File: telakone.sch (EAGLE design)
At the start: 180 parts, among them X10 MPT0.5/8-2.54, X11 MPT0.5/8-2.54, X2 MPT0.5/8-2.54, X3 MPT0.5/8-2.54, X4 PIIKKIRIMA-2, X5 PIIKKIRIMA-5, X7 U.FL-R-SMT-1, X8 MPT0.5/8-2.54, Y1 PTH2.6-5.5SQ, Y2 PTH2.6-5.5SQ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

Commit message: Layout finished
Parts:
- added H1: RED, omat_ic_2:LEDCHIP-LED0603
- added H2, H3: GRN, omat_ic_2:LEDCHIP-LED0603
- added R18, R24, R25: (no value), omat_ic_2:RES0603
- added U$1: DAFUG, dafug:DAFUG
- added X9: PIIKKIRIMA-3, omat_ic_2:PIIKKIRIMA-3
- added Y5: PTH2.6-5.5SQ, EKE:PTH2.6-5.5SQ
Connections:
- new net N$23: H2.C, R24.2
- new net N$25: H1.C, R18.2
- new net N$26: D1G$2.PB8, H1.A
- new net N$27: D1G$2.PB9, H2.A
- new net N$28: H3.C, R25.2
- new net USART1CTS: A1.UART1_RTSL, D1G$2.PA11
- new net USART1RTS: A1.UART1_CTSL, D1G$2.PA12
- new net USART1RX: A1.UART1_TX, D1G$2.PA10
- new net USART1TX: A1.UART1_RX, D1G$2.PA9
- new net USART3RX: D1G$2.PD9, X9.2
- new net USART3TX: D1G$2.PD8, X9.3
- net +3V3: now also H3.A
- net GND: now also R18.1, R24.1, R25.1, X9.1, Y5.1
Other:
- note added: "USART1"
- note added: "USART3"
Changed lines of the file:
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@@
 <part name="GND46" library="EKE" deviceset="GND" device=""/>
 <part name="+3V8" library="EKE" deviceset="+3V3" device=""/>
+<part name="X9" library="omat_ic_2" deviceset="PIIKKIRIMA-3" device=""/>
+<part name="GND85" library="EKE" deviceset="GND" device=""/>
+<part name="H1" library="omat_ic_2" deviceset="LED" device="CHIP-LED0603" value="RED"/>
+<part name="H2" library="omat_ic_2" deviceset="LED" device="CHIP-LED0603" value="GRN"/>
+<part name="R18" library="omat_ic_2" deviceset="RES" device="0603"/>
+<part name="R24" library="omat_ic_2" deviceset="RES" device="0603"/>
+<part name="GND86" library="EKE" deviceset="GND" device=""/>
+<part name="GND87" library="EKE" deviceset="GND" device=""/>
+<part name="H3" library="omat_ic_2" deviceset="LED" device="CHIP-LED0603" value="GRN"/>
+<part name="R25" library="omat_ic_2" deviceset="RES" device="0603"/>
+<part name="GND88" library="EKE" deviceset="GND" device=""/>
+<part name="+3V23" library="EKE" deviceset="+3V3" device=""/>
+<part name="U$1" library="dafug" deviceset="DAFUG" device=""/>
+<part name="Y5" library="EKE" deviceset="PTH" device="2.6-5.5SQ"/>
+<part name="U$2" library="dafug" deviceset="OSHW" device=""/>
 </parts>
 <sheets>
@@
 <instance part="Y3" gate="G$1" x="106.68" y="35.56"/>
 <instance part="Y4" gate="G$1" x="106.68" y="25.4"/>
-<instance part="GND77" gate="1" x="96.52" y="20.32"/>
+<instance part="GND77" gate="1" x="96.52" y="10.16"/>
+<instance part="U$1" gate="G$1" x="292.1" y="30.48"/>
+<instance part="Y5" gate="G$1" x="106.68" y="15.24"/>
+<instance part="U$2" gate="G$1" x="320.04" y="40.64"/>
 </instances>
 <busses>
@@
 <wire x1="96.52" y1="45.72" x2="96.52" y2="35.56" width="0.1524" layer="91"/>
 <wire x1="96.52" y1="35.56" x2="96.52" y2="25.4" width="0.1524" layer="91"/>
-<wire x1="96.52" y1="25.4" x2="96.52" y2="22.86" width="0.1524" layer="91"/>
+<wire x1="96.52" y1="25.4" x2="96.52" y2="15.24" width="0.1524" layer="91"/>
+<wire x1="96.52" y1="15.24" x2="96.52" y2="12.7" width="0.1524" layer="91"/>
 <wire x1="99.06" y1="25.4" x2="96.52" y2="25.4" width="0.1524" layer="91"/>
 <junction x="96.52" y="25.4"/>
@@
 <wire x1="99.06" y1="45.72" x2="96.52" y2="45.72" width="0.1524" layer="91"/>
 <junction x="96.52" y="45.72"/>
+<pinref part="Y5" gate="G$1" pin="1"/>
+<wire x1="99.06" y1="15.24" x2="96.52" y2="15.24" width="0.1524" layer="91"/>
+<junction x="96.52" y="15.24"/>
 </segment>
 </net>
@@
 <text x="251.46" y="193.04" size="1.778" layer="97">TIM9_CH1
 TIM9_CH2</text>
-<text x="88.9" y="147.32" size="1.778" layer="97">SPI2</text>
+<text x="88.9" y="144.78" size="1.778" layer="97">SPI2</text>
 <text x="203.2" y="185.42" size="1.778" layer="97">SPI3</text>
 <text x="88.9" y="162.56" size="1.778" layer="97">I2C1</text>
@@
 <text x="200.66" y="139.7" size="1.778" layer="97">TIM4_CH2</text>
 <text x="200.66" y="160.02" size="1.778" layer="97">USART2</text>
+<text x="86.36" y="185.42" size="1.778" layer="97">USART1</text>
+<text x="236.22" y="144.78" size="1.778" layer="97" rot="R90">USART3</text>
 </plain>
 <instances>
@@
 <instance part="GND53" gate="1" x="200.66" y="53.34"/>
 <instance part="+3V31" gate="G$1" x="200.66" y="66.04"/>
+<instance part="X9" gate="G$1" x="226.06" y="149.86" rot="R180"/>
+<instance part="GND85" gate="1" x="218.44" y="142.24"/>
+<instance part="H1" gate="G$1" x="71.12" y="149.86"/>
+<instance part="H2" gate="G$1" x="81.28" y="149.86"/>
+<instance part="R18" gate="G$1" x="71.12" y="139.7" rot="R90"/>
+<instance part="R24" gate="G$1" x="81.28" y="139.7" rot="R90"/>
+<instance part="GND86" gate="1" x="71.12" y="132.08"/>
+<instance part="GND87" gate="1" x="81.28" y="132.08"/>
+<instance part="H3" gate="G$1" x="60.96" y="149.86"/>
+<instance part="R25" gate="G$1" x="60.96" y="139.7" rot="R90"/>
+<instance part="GND88" gate="1" x="60.96" y="132.08"/>
+<instance part="+3V23" gate="G$1" x="60.96" y="160.02"/>
 </instances>
 <busses>
@@
 <pinref part="GND53" gate="1" pin="GND"/>
 </segment>
+<segment>
+<pinref part="X9" gate="G$1" pin="1"/>
+<wire x1="220.98" y1="147.32" x2="218.44" y2="147.32" width="0.1524" layer="91"/>
+<wire x1="218.44" y1="147.32" x2="218.44" y2="144.78" width="0.1524" layer="91"/>
+<pinref part="GND85" gate="1" pin="GND"/>
+</segment>
+<segment>
+<pinref part="GND87" gate="1" pin="GND"/>
+<pinref part="R24" gate="G$1" pin="1"/>
+</segment>
+<segment>
+<pinref part="R18" gate="G$1" pin="1"/>
+<pinref part="GND86" gate="1" pin="GND"/>
+</segment>
+<segment>
+<pinref part="R25" gate="G$1" pin="1"/>
+<pinref part="GND88" gate="1" pin="GND"/>
+</segment>
 </net>
 <net name="+3V3" class="0">
@@
 <pinref part="+3V31" gate="G$1" pin="+3V3"/>
 </segment>
+<segment>
+<pinref part="+3V23" gate="G$1" pin="+3V3"/>
+<pinref part="H3" gate="G$1" pin="A"/>
+<wire x1="60.96" y1="157.48" x2="60.96" y2="152.4" width="0.1524" layer="91"/>
+</segment>
 </net>
 <net name="I2C1SCL" class="0">
@@
 </segment>
 </net>
+<net name="USART1TX" class="0">
+<segment>
+<pinref part="D1" gate="G$2" pin="PA9"/>
+<wire x1="127" y1="190.5" x2="99.06" y2="190.5" width="0.1524" layer="91"/>
+<label x="101.6" y="190.5" size="1.778" layer="95"/>
+</segment>
+</net>
+<net name="USART1RX" class="0">
+<segment>
+<pinref part="D1" gate="G$2" pin="PA10"/>
+<wire x1="127" y1="187.96" x2="99.06" y2="187.96" width="0.1524" layer="91"/>
+<label x="101.6" y="187.96" size="1.778" layer="95"/>
+</segment>
+</net>
+<net name="USART1CTS" class="0">
+<segment>
+<pinref part="D1" gate="G$2" pin="PA11"/>
+<wire x1="127" y1="185.42" x2="99.06" y2="185.42" width="0.1524" layer="91"/>
+<label x="101.6" y="185.42" size="1.778" layer="95"/>
+</segment>
+</net>
+<net name="USART1RTS" class="0">
+<segment>
+<pinref part="D1" gate="G$2" pin="PA12"/>
+<wire x1="127" y1="182.88" x2="99.06" y2="182.88" width="0.1524" layer="91"/>
+<label x="101.6" y="182.88" size="1.778" layer="95"/>
+</segment>
+</net>
+<net name="USART3TX" class="0">
+<segment>
+<pinref part="D1" gate="G$2" pin="PD8"/>
+<label x="182.88" y="152.4" size="1.778" layer="95"/>
+<pinref part="X9" gate="G$1" pin="3"/>
+<wire x1="175.26" y1="152.4" x2="220.98" y2="152.4" width="0.1524" layer="91"/>
+</segment>
+</net>
+<net name="USART3RX" class="0">
+<segment>
+<pinref part="D1" gate="G$2" pin="PD9"/>
+<label x="182.88" y="149.86" size="1.778" layer="95"/>
+<pinref part="X9" gate="G$1" pin="2"/>
+<wire x1="220.98" y1="149.86" x2="175.26" y2="149.86" width="0.1524" layer="91"/>
+</segment>
+</net>
+<net name="N$23" class="0">
+<segment>
+<pinref part="R24" gate="G$1" pin="2"/>
+<pinref part="H2" gate="G$1" pin="C"/>
+</segment>
+</net>
+<net name="N$25" class="0">
+<segment>
+<pinref part="H1" gate="G$1" pin="C"/>
+<pinref part="R18" gate="G$1" pin="2"/>
+</segment>
+</net>
+<net name="N$26" class="0">
+<segment>
+<pinref part="D1" gate="G$2" pin="PB8"/>
+<pinref part="H1" gate="G$1" pin="A"/>
+<wire x1="127" y1="160.02" x2="71.12" y2="160.02" width="0.1524" layer="91"/>
+<wire x1="71.12" y1="160.02" x2="71.12" y2="152.4" width="0.1524" layer="91"/>
+</segment>
+</net>
+<net name="N$27" class="0">
+<segment>
+<pinref part="D1" gate="G$2" pin="PB9"/>
+<pinref part="H2" gate="G$1" pin="A"/>
+<wire x1="127" y1="157.48" x2="81.28" y2="157.48" width="0.1524" layer="91"/>
+<wire x1="81.28" y1="157.48" x2="81.28" y2="152.4" width="0.1524" layer="91"/>
+</segment>
+</net>
+<net name="N$28" class="0">
+<segment>
+<pinref part="H3" gate="G$1" pin="C"/>
+<pinref part="R25" gate="G$1" pin="2"/>
+</segment>
+</net>
 </nets>
 </sheet>
@@
 </segment>
 </net>
+<net name="USART1RX" class="0">
+<segment>
+<pinref part="A1" gate="G$1" pin="UART1_TX"/>
+<wire x1="226.06" y1="142.24" x2="246.38" y2="142.24" width="0.1524" layer="91"/>
+<label x="233.68" y="142.24" size="1.778" layer="95"/>
+</segment>
+</net>
+<net name="USART1TX" class="0">
+<segment>
+<pinref part="A1" gate="G$1" pin="UART1_RX"/>
+<wire x1="226.06" y1="139.7" x2="246.38" y2="139.7" width="0.1524" layer="91"/>
+<label x="233.68" y="139.7" size="1.778" layer="95"/>
+</segment>
+</net>
+<net name="USART1CTS" class="0">
+<segment>
+<pinref part="A1" gate="G$1" pin="UART1_RTSL"/>
+<wire x1="226.06" y1="137.16" x2="246.38" y2="137.16" width="0.1524" layer="91"/>
+<label x="233.68" y="137.16" size="1.778" layer="95"/>
+</segment>
+</net>
+<net name="USART1RTS" class="0">
+<segment>
+<pinref part="A1" gate="G$1" pin="UART1_CTSL"/>
+<wire x1="226.06" y1="134.62" x2="246.38" y2="134.62" width="0.1524" layer="91"/>
+<label x="233.68" y="134.62" size="1.778" layer="95"/>
+</segment>
+</net>

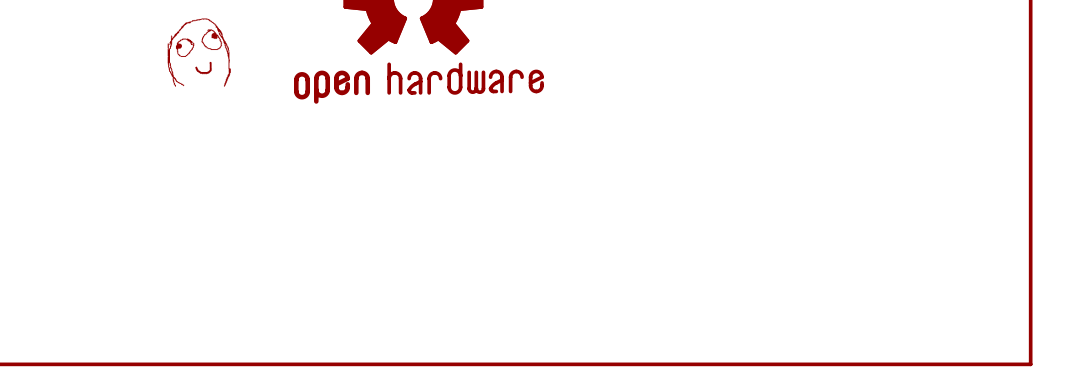
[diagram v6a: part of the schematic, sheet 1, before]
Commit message: add version label to board
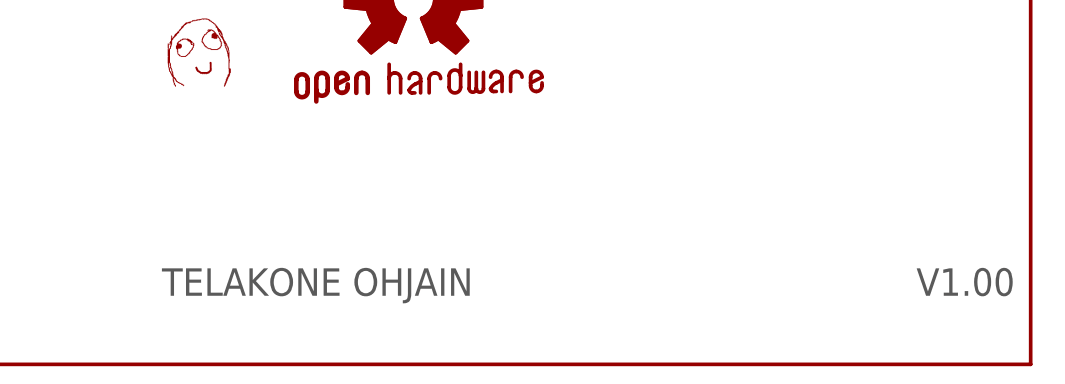
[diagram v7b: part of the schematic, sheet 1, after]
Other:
- note added: "TELAKONE OHJAIN"
- note added: "V1.00"
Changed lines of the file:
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@@
 <plain>
 <text x="93.98" y="66.04" size="1.778" layer="97">MOUNTING HOLES</text>
+<text x="375.92" y="7.62" size="3.048" layer="97">V1.00</text>
+<text x="292.1" y="7.62" size="3.048" layer="97">TELAKONE OHJAIN</text>
 </plain>
 <instances>

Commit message: update documentation
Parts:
- added U$11, U$13, U$15, U$3, U$5, U$7, U$9: DAFUG, dafug:DAFUG
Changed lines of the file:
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@@
 <part name="Y5" library="EKE" deviceset="PTH" device="2.6-5.5SQ"/>
 <part name="U$2" library="dafug" deviceset="OSHW" device=""/>
+<part name="U$3" library="dafug" deviceset="DAFUG" device=""/>
+<part name="U$4" library="dafug" deviceset="OSHW" device=""/>
+<part name="U$5" library="dafug" deviceset="DAFUG" device=""/>
+<part name="U$6" library="dafug" deviceset="OSHW" device=""/>
+<part name="U$7" library="dafug" deviceset="DAFUG" device=""/>
+<part name="U$8" library="dafug" deviceset="OSHW" device=""/>
+<part name="U$9" library="dafug" deviceset="DAFUG" device=""/>
+<part name="U$10" library="dafug" deviceset="OSHW" device=""/>
+<part name="U$11" library="dafug" deviceset="DAFUG" device=""/>
+<part name="U$12" library="dafug" deviceset="OSHW" device=""/>
+<part name="U$13" library="dafug" deviceset="DAFUG" device=""/>
+<part name="U$14" library="dafug" deviceset="OSHW" device=""/>
+<part name="U$15" library="dafug" deviceset="DAFUG" device=""/>
+<part name="U$16" library="dafug" deviceset="OSHW" device=""/>
 </parts>
 <sheets>
@@
 <plain>
 <text x="43.18" y="93.98" size="1.778" layer="97">~1.2mA/LSB</text>
+<text x="375.92" y="7.62" size="3.048" layer="97">V1.00</text>
+<text x="292.1" y="7.62" size="3.048" layer="97">TELAKONE OHJAIN</text>
 </plain>
 <instances>
@@
 <instance part="C53" gate="G$1" x="287.02" y="203.2"/>
 <instance part="GND80" gate="1" x="287.02" y="195.58"/>
+<instance part="U$3" gate="G$1" x="292.1" y="30.48"/>
+<instance part="U$4" gate="G$1" x="320.04" y="40.64"/>
 </instances>
 <busses>
@@
 MAX INPUT 20V</text>
 <text x="284.48" y="144.78" size="1.778" layer="97" rot="R90">SPEED SENSORS</text>
+<text x="375.92" y="7.62" size="3.048" layer="97">V1.00</text>
+<text x="292.1" y="7.62" size="3.048" layer="97">TELAKONE OHJAIN</text>
 </plain>
 <instances>
@@
 <instance part="GND78" gate="1" x="266.7" y="172.72"/>
 <instance part="V28" gate="G$1" x="309.88" y="127"/>
+<instance part="U$5" gate="G$1" x="292.1" y="30.48"/>
+<instance part="U$6" gate="G$1" x="320.04" y="40.64"/>
 </instances>
 <busses>
@@
 <text x="147.32" y="76.2" size="1.778" layer="97">GAIN=2
 ~1.22 mV/LSB</text>
+<text x="375.92" y="7.62" size="3.048" layer="97">V1.00</text>
+<text x="292.1" y="7.62" size="3.048" layer="97">TELAKONE OHJAIN</text>
 </plain>
 <instances>
@@
 <instance part="C56" gate="G$1" x="25.4" y="170.18" rot="MR0"/>
 <instance part="GND83" gate="1" x="25.4" y="162.56"/>
+<instance part="U$7" gate="G$1" x="292.1" y="30.48"/>
+<instance part="U$8" gate="G$1" x="320.04" y="40.64"/>
 </instances>
 <busses>
@@
 <text x="147.32" y="76.2" size="1.778" layer="97">GAIN=2
 ~1.22 mV/LSB</text>
+<text x="375.92" y="7.62" size="3.048" layer="97">V1.00</text>
+<text x="292.1" y="7.62" size="3.048" layer="97">TELAKONE OHJAIN</text>
 </plain>
 <instances>
@@
 <instance part="C57" gate="G$1" x="25.4" y="170.18" rot="MR0"/>
 <instance part="GND84" gate="1" x="25.4" y="162.56"/>
+<instance part="U$9" gate="G$1" x="292.1" y="30.48"/>
+<instance part="U$10" gate="G$1" x="320.04" y="40.64"/>
 </instances>
 <busses>
@@
 ~4.97mV/LSB
 ADC123_in0</text>
+<text x="375.92" y="7.62" size="3.048" layer="97">V1.00</text>
+<text x="292.1" y="7.62" size="3.048" layer="97">TELAKONE OHJAIN</text>
 </plain>
 <instances>
@@
 <instance part="GND46" gate="1" x="345.44" y="160.02"/>
 <instance part="+3V8" gate="G$1" x="345.44" y="172.72"/>
+<instance part="U$11" gate="G$1" x="292.1" y="30.48"/>
+<instance part="U$12" gate="G$1" x="320.04" y="40.64"/>
 </instances>
 <busses>
@@
 <text x="86.36" y="185.42" size="1.778" layer="97">USART1</text>
 <text x="236.22" y="144.78" size="1.778" layer="97" rot="R90">USART3</text>
+<text x="375.92" y="7.62" size="3.048" layer="97">V1.00</text>
+<text x="292.1" y="7.62" size="3.048" layer="97">TELAKONE OHJAIN</text>
 </plain>
 <instances>
@@
 <instance part="GND88" gate="1" x="60.96" y="132.08"/>
 <instance part="+3V23" gate="G$1" x="60.96" y="160.02"/>
+<instance part="U$13" gate="G$1" x="292.1" y="30.48"/>
+<instance part="U$14" gate="G$1" x="320.04" y="40.64"/>
 </instances>
 <busses>
@@
 <description>WIFI</description>
 <plain>
+<text x="375.92" y="7.62" size="3.048" layer="97">V1.00</text>
+<text x="292.1" y="7.62" size="3.048" layer="97">TELAKONE OHJAIN</text>
 </plain>
 <instances>
@@
 <instance part="GND56" gate="1" x="129.54" y="157.48"/>
 <instance part="+3V34" gate="G$1" x="129.54" y="170.18"/>
+<instance part="U$15" gate="G$1" x="292.1" y="30.48"/>
+<instance part="U$16" gate="G$1" x="320.04" y="40.64"/>
 </instances>
 <busses>
